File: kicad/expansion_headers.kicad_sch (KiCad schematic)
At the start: 16 parts, among them J12 Conn_02x17_Odd_Even, J13 Conn_02x17_Odd_Even, U105 74LS245, U106 74LS244

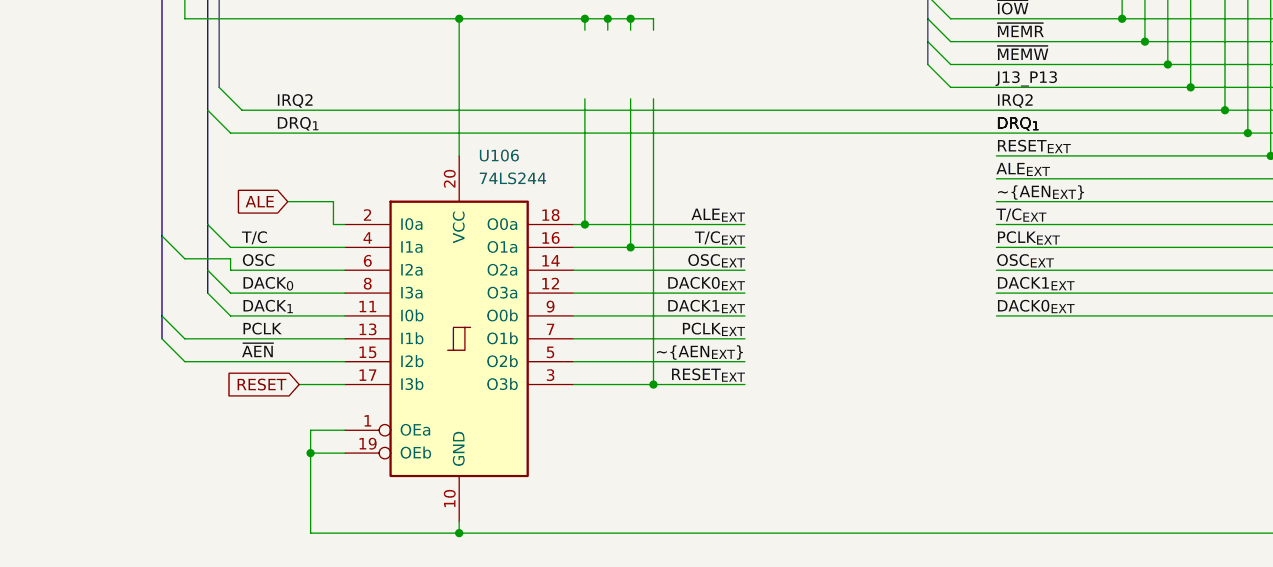
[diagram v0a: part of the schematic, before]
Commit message: Fixes to clocks,  keyboard controller stuff.
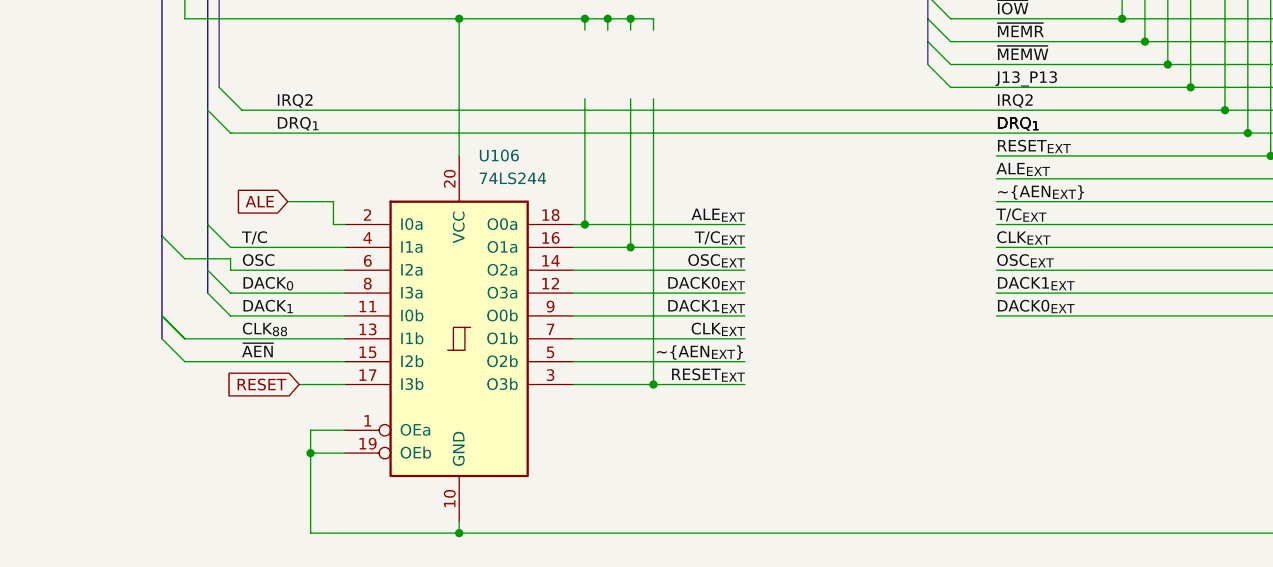
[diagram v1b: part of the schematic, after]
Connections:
- net PCLK renamed CLK_{88}
- net PCLK_{EXT} renamed CLK_{EXT}
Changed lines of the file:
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@@
 	)
 	(bus_entry
+		(at 31.75 161.29)
+		(size 2.54 2.54)
+		(stroke
+			(width 0)
+			(type default)
+		)
+	)
+	(bus_entry
 		(at 40.64 46.99)
 		(size 2.54 2.54)
@@
 		)
 	)
-	(bus
+	(wire
 		(pts
-			(xy 40.64 26.67) (xy 189.23 26.67)
+			(xy 34.29 163.83) (xy 52.07 163.83)
 		)
 		(stroke
-			(width 1)
+			(width 0)
 			(type default)
-			(color 0 0 194 1)
 		)
 	)
-	(wire
+	(bus
 		(pts
-			(xy 34.29 163.83) (xy 52.07 163.83)
+			(xy 40.64 26.67) (xy 189.23 26.67)
 		)
 		(stroke
-			(width 0)
+			(width 1)
 			(type default)
+			(color 0 0 194 1)
 		)
 	)
@@
 		)
 	)
+	(label "CLK_{88}"
+		(at 40.64 163.83 0)
+		(effects
+			(font
+				(size 1.27 1.27)
+			)
+			(justify left bottom)
+		)
+	)
 	(label "XA14"
 		(at 58.42 64.77 0)
@@
 		)
 	)
-	(label "PCLK"
-		(at 40.64 163.83 0)
-		(effects
-			(font
-				(size 1.27 1.27)
-			)
-			(justify left bottom)
-		)
-	)
 	(label "ALE_{EXT}"
 		(at 96.52 151.13 180)
@@
 		)
 	)
-	(label "PCLK_{EXT}"
+	(label "CLK_{EXT}"
 		(at 96.52 163.83 180)
 		(effects
@@
 		)
 	)
-	(label "PCLK_{EXT}"
+	(label "CLK_{EXT}"
 		(at 124.46 153.67 0)
 		(effects

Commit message: update kicad project
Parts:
- C101, C102, RN20: seq_coord (none) -> J8
- C103, RN22: seq_coord (none) -> J7
- C97: seq_coord (none) -> K4
- C98: seq_coord (none) -> J1
- J12, RN17: seq_coord (none) -> J2
- J13: seq_coord (none) -> I7
- RN16: seq_coord (none) -> J3
- RN18: seq_coord (none) -> I3
- RN19: seq_coord (none) -> K5
- RN21: seq_coord (none) -> I8
- U105: seq_coord (none) -> I7; seq_silkscreen (none) -> LS245
- U106: seq_coord (none) -> I9; seq_silkscreen (none) -> LS244
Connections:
- net +5V: now also C101.1, C102.1, C97.1, C98.1, RN18.1 (R1), RN19.1 (R1), RN21.1 (R1), RN21.1 (R1), RN21.1 (R1), RN21.1 (R1), RN22.1 (R1), RN22.1 (R1), RN22.1 (R1)
- net CLK_{EXT}: now also RN21.8 (R7.2)
- net GND: now also C101.2, C102.2, C97.2, C98.2
- net OSC_{EXT}: no longer RN21.8 (R7.2)
- net J13_P1 renamed IO_CH_READY
- net J13_P13 renamed NMI_P3
- net NMI_PAL_{I9} renamed ~{IO_CH_CK}
- no-connect marks 3 -> 6
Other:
- moved on the sheet: C101, C102, C103, C97, C98, RN21G, RN22B, RN22C

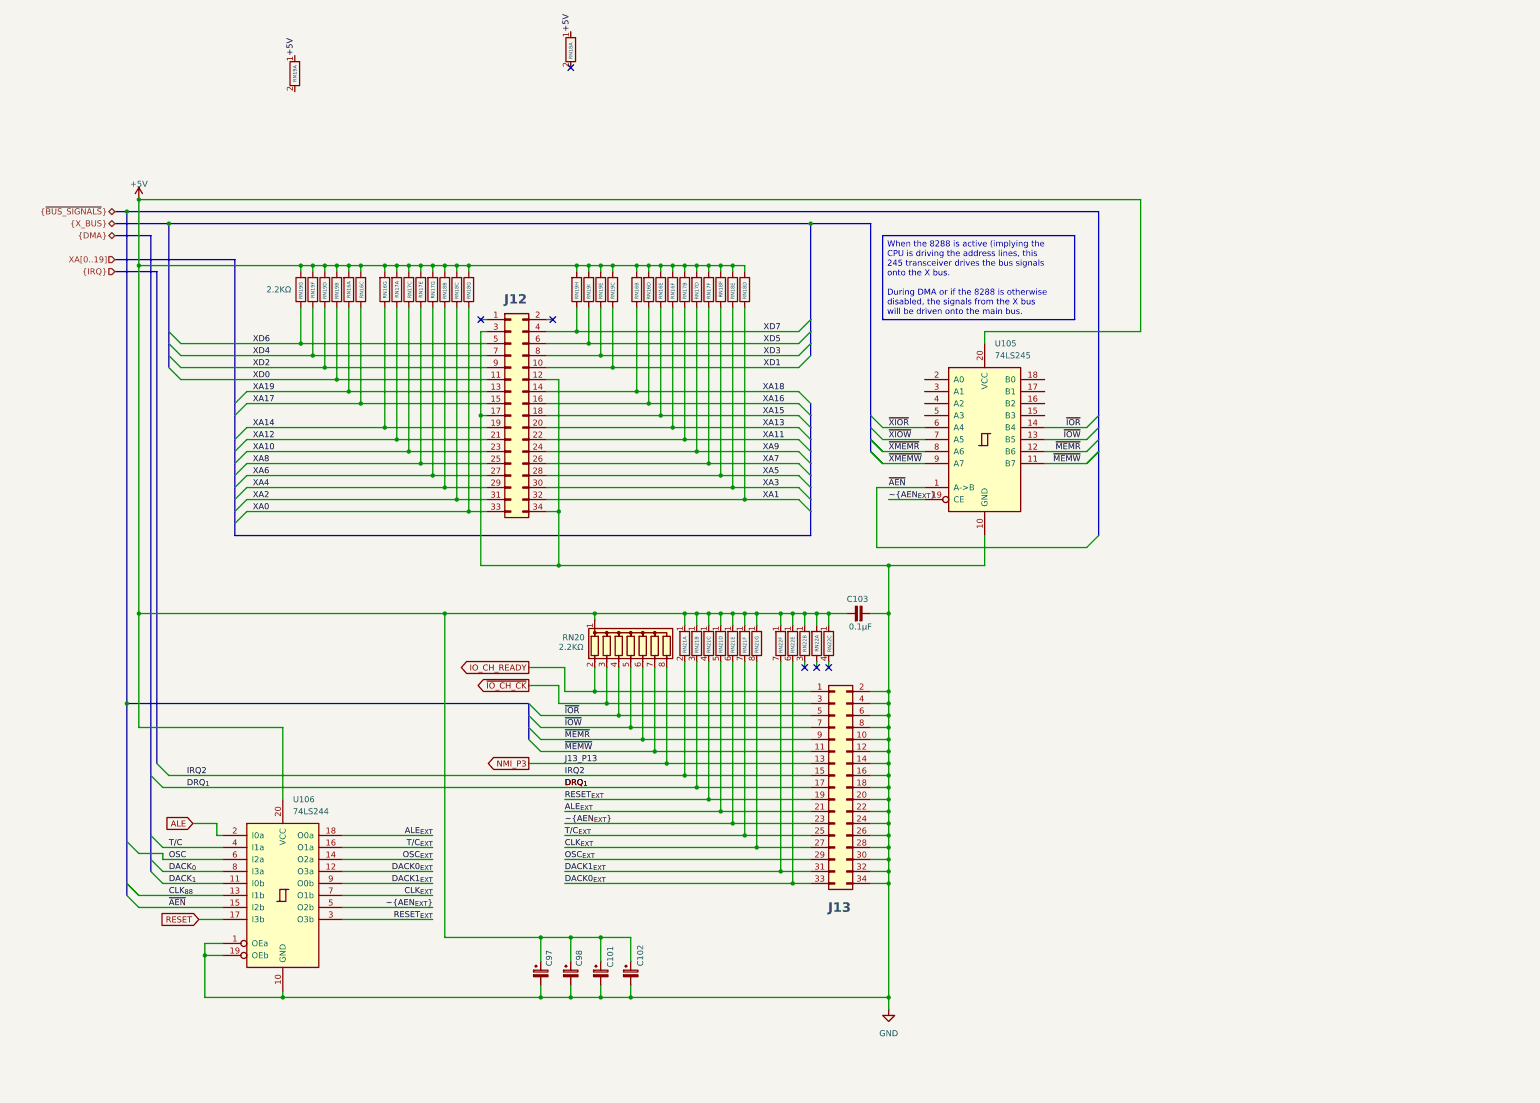
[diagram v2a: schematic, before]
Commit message: Add parallel port, game port
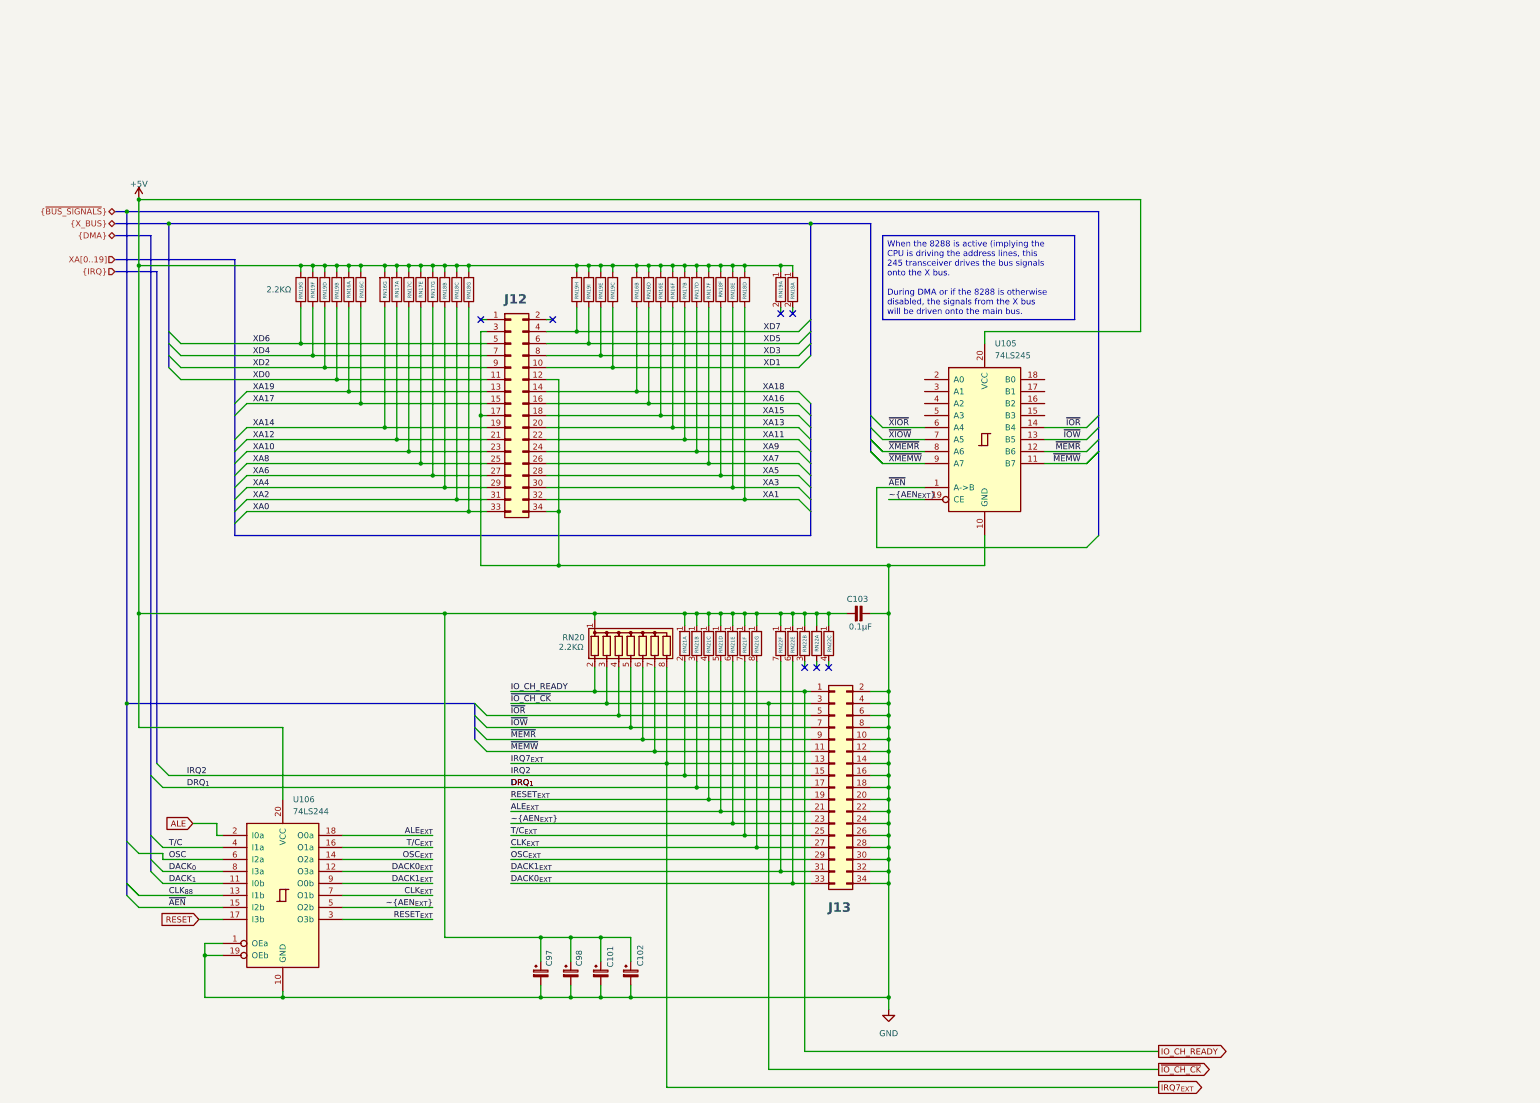
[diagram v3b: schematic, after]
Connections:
- net NMI_P3 renamed IRQ7_{EXT}
- no-connect marks 6 -> 7
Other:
- moved on the sheet: RN18A, RN19A

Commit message: Updates, chameleon logo
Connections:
- net RESET renamed RESET_{BRD}
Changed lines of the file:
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@@
 		)
 	)
-	(global_label "RESET"
+	(global_label "RESET_{BRD}"
 		(shape input)
 		(at 46.99 168.91 180)
